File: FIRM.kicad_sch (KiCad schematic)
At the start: 93 parts, among them J1 DM3CS-SF, J2 Conn_01x02_Pin, Q1 IRLML6402, U1 W25Q128JVP, U2 STM32F405RGTx, U3 ADXL371, U5 INA219AxDCN, U6 MIC5219-3.3YM5, U9 A-USBC-20F0-EA-GSR05, X1 32.768khz, Y1 12 MHz

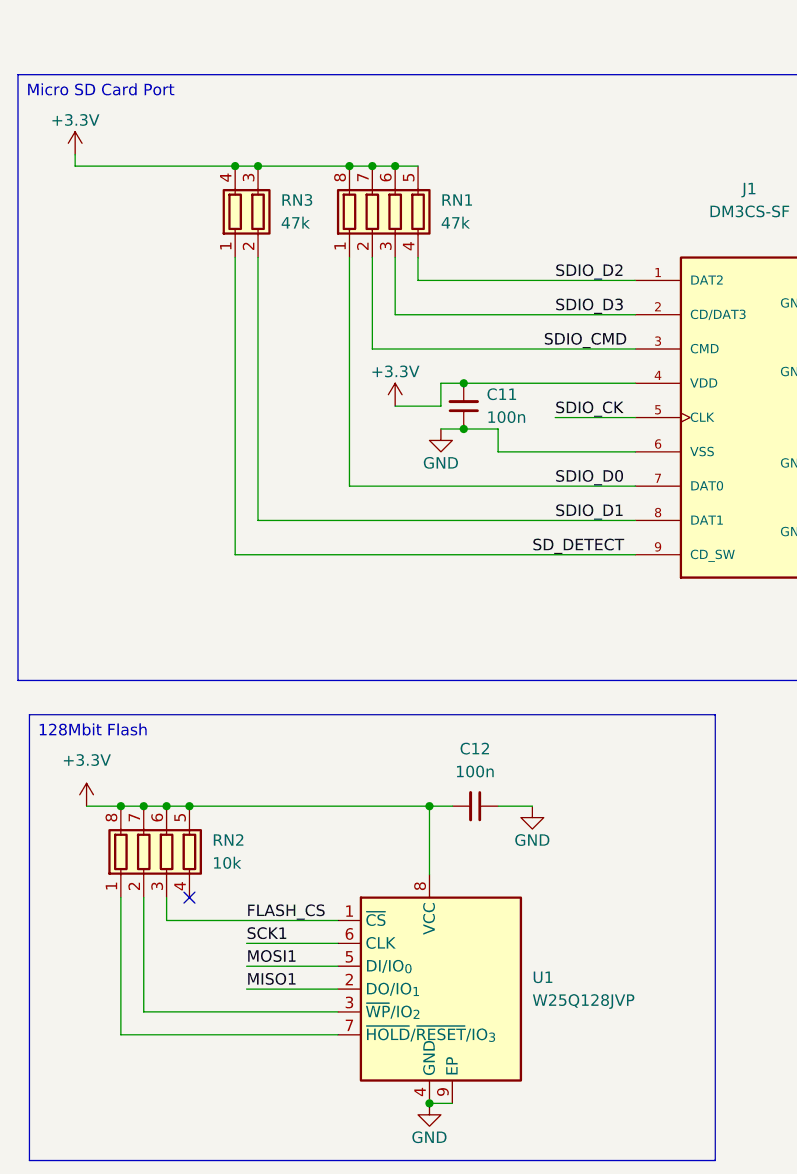
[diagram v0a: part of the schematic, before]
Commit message: cleanup and improved decoupling capacitor locations
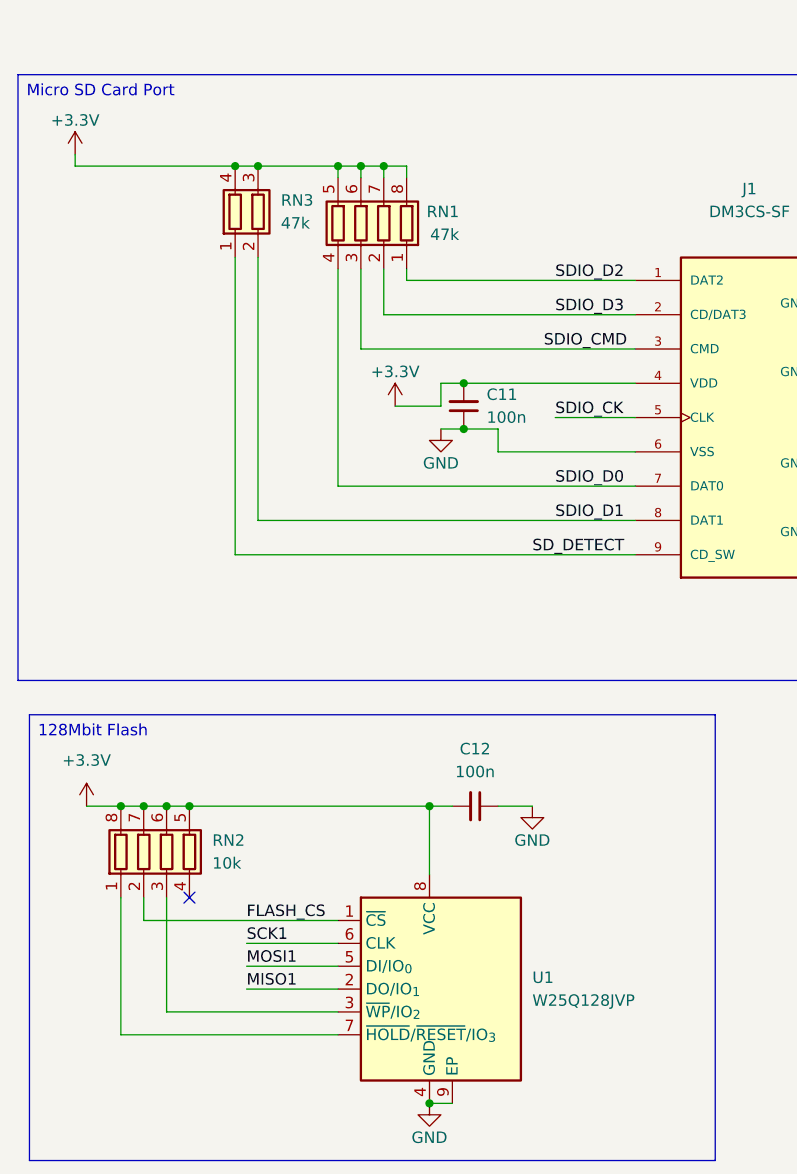
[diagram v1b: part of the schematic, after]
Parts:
- U1: footprint Package_SON:WSON-8-1EP_6x5mm_P1.27mm_EP3.4x4.3mm -> Package_SO:SOIC-8_5.3x5.3mm_P1.27mm
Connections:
- net FLASH_CS: now also RN2.2 (R2.1); no longer RN2.3 (R3.1)
- net SDIO_CMD: now also RN1.3 (R3.1); no longer RN1.2 (R2.1)
- net SDIO_D0: now also RN1.4 (R4.1); no longer RN1.1 (R1.1)
- net SDIO_D2: now also RN1.1 (R1.1); no longer RN1.4 (R4.1)
- net SDIO_D3: now also RN1.2 (R2.1); no longer RN1.3 (R3.1)
- net at U1.3 (~{WP}/IO_{2}): now also RN2.3 (R3.1); no longer RN2.2 (R2.1)
- new net: U3.10 (RES), U3.13 (GND), U3.16 (GND)
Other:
- moved on the sheet: RN1

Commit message: added back resistors
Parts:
- removed RN1: 47k, connectors:R_Array_YC104, symbol Device:R_Pack04
- removed RN3: 47k, connectors:R_Array_EXB-24V, symbol Device:R_Pack02
- removed U1: W25Q128JVP, Package_SO:SOIC-8_5.3x5.3mm_P1.27mm, symbol Memory_Flash:W25Q128JVP
- added R1, R2, R4, R5, R6, R7: 47k, Resistor_SMD:R_0402_1005Metric, symbol Device:R_Small
- added U1: W25Q128JVS, Package_SO:SOIC-8_5.3x5.3mm_P1.27mm, symbol Memory_Flash:W25Q128JVS
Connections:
- net +3.3V: now also R1.2, R2.2, R4.2, R5.2, R6.2, R7.2, U1.8 (VCC)
- net FLASH_CS: now also U1.1 (~{CS})
- net GND: now also U1.4 (GND)
- net MISO1: now also U1.2 (DO/IO_{1})
- net MOSI1: now also U1.5 (DI/IO_{0})
- net SCK1: now also U1.6 (CLK)
- net SDIO_CMD: now also R4.1
- net SDIO_D0: now also R5.1
- net SDIO_D1: now also R6.1
- net SDIO_D2: now also R1.1
- net SDIO_D3: now also R2.1
- net SD_DETECT: now also R7.1
- net at RN2.1 (R1.1): now also U1.7 (~{HOLD}/~{RESET}/IO_{3})
- net at RN2.3 (R3.1): now also U1.3 (~{WP}/IO_{2})
- new net: U3.10 (RES), U3.13 (GND), U3.16 (GND)

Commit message: part numbers
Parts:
- C1, C17: value 0.1u -> 100n; Digikey PN 399-C0603C104K5RACTUCT-ND -> 1276-1043-1-ND
- C10, C5: Digikey PN 311-1767-1-ND -> 490-GJM1555C1H140FB01DCT-ND
- C11, C12, C13, C15, C19, C20, C21, C22, C23, C25, C27, C3, C6, C8: Digikey PN 399-C0603C104K5RACTUCT-ND -> 1276-1043-1-ND
- C14, C9: Digikey PN 490-4520-1-ND -> 490-10012-1-ND
- C16: Digikey PN 399-C0603C103K5RACTUCT-ND -> 490-1313-1-ND
- C18, C29: Digikey PN 587-1241-1-ND -> 1276-1067-1-ND
- C2: Digikey PN 1276-1044-1-ND -> 1276-1482-1-ND
- C24, C28, C30: Digikey PN 490-18214-1-ND -> 1276-1451-1-ND
- C26: Digikey PN 1276-1168-1-ND -> 490-1300-1-ND
- C4, C7: Digikey PN 1276-2134-1-ND -> 311-3714-1-ND
- D1: Digikey PN 160-1645-1-ND -> 160-LTST-C281TBKTCT-ND
- D2: Digikey PN 160-1428-1-ND -> 160-LTST-C281KSKTCT-ND
- D3: Digikey PN 160-1422-1-ND -> 160-LTST-C281KRKTCT-ND
- D5: Digikey PN 160-1423-1-ND -> 160-LTST-C281KGKTCT-ND
- R1, R2, R4, R5, R6, R7: Digikey PN 311-2.20KHRCT-ND -> 311-47.0KLRCT-ND
- R11, R12: Digikey PN 311-2.20KHRCT-ND -> P3.3KDCCT-ND
- R13: Digikey PN 311-330HRCT-ND -> 311-330LRCT-ND
- R14, R18: Digikey PN P1.2KDBCT-ND -> 311-1.2KJRCT-ND
- R15: Digikey PN 311-1.50KHRCT-ND -> 311-1.50KLRCT-ND
- R16, R3: Digikey PN 311-100KHRCT-ND -> P100KLCT-ND
- R17: value 0.01R -> 10m; Digikey PN (none) -> P19181CT-ND
- R19: Digikey PN 541-100HCT-ND -> P100LCT-ND
- R20, R21: Digikey PN 311-5.10KHRCT-ND -> P5.1KDCCT-ND
- RN2: Digikey PN (none) -> 13-YC104-FR-0710KLCT-ND
- U1: Digikey PN (none) -> 256-W25Q128JVSIQTRCT-ND
- U3: Digikey PN (none) -> 505-ADXL371BCCZ-RL7CT-ND
- U5: Digikey PN (none) -> 296-23770-1-ND
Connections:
- new net: U3.10 (RES), U3.13 (GND), U3.16 (GND)
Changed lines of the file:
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@@
 			)
 		)
+		(property "Digikey PN" "256-W25Q128JVSIQTRCT-ND"
+			(at 60.96 260.35 0)
+			(effects
+				(font
+					(size 1.27 1.27)
+				)
+				(hide yes)
+			)
+		)
 		(pin "1"
 		)
@@
 			)
 		)
-		(property "Digikey PN" "399-C0603C104K5RACTUCT-ND"
+		(property "Digikey PN" "1276-1043-1-ND"
 			(at 87.63 41.91 0)
 			(effects
@@
 			)
 		)
-		(property "Digikey PN" "399-C0603C104K5RACTUCT-ND"
+		(property "Digikey PN" "1276-1043-1-ND"
 			(at 36.83 41.91 0)
 			(effects
@@
 			)
 		)
-		(property "Digikey PN" "311-100KHRCT-ND"
+		(property "Digikey PN" "P100KLCT-ND"
 			(at 30.48 66.04 0)
 			(effects
@@
 			)
 		)
-		(property "Digikey PN" "490-18214-1-ND"
+		(property "Digikey PN" "1276-1451-1-ND"
 			(at 340.36 224.79 0)
 			(effects
@@
 			)
 		)
-		(property "Value" "0.1u"
+		(property "Value" "100n"
 			(at 22.098 62.23 0)
 			(effects
@@
 			)
 		)
-		(property "Digikey PN" "399-C0603C104K5RACTUCT-ND"
+		(property "Digikey PN" "1276-1043-1-ND"
 			(at 19.05 60.96 0)
 			(effects
@@
 			)
 		)
-		(property "Digikey PN" "399-C0603C104K5RACTUCT-ND"
+		(property "Digikey PN" "1276-1043-1-ND"
 			(at 285.75 105.41 0)
 			(effects
@@
 			)
 		)
-		(property "Digikey PN" "160-1428-1-ND"
+		(property "Digikey PN" "160-LTST-C281KSKTCT-ND"
 			(at 191.77 116.84 0)
 			(effects
@@
 			)
 		)
-		(property "Digikey PN" "399-C0603C104K5RACTUCT-ND"
+		(property "Digikey PN" "1276-1043-1-ND"
 			(at 64.77 195.58 0)
 			(effects
@@
 			)
 		)
-		(property "Digikey PN" "311-2.20KHRCT-ND"
+		(property "Digikey PN" "P3.3KDCCT-ND"
 			(at 153.67 111.76 0)
 			(effects
@@
 			)
 		)
-		(property "Digikey PN" "399-C0603C104K5RACTUCT-ND"
+		(property "Digikey PN" "1276-1043-1-ND"
 			(at 66.04 240.03 90)
 			(effects
@@
 			)
 		)
-		(property "Digikey PN" "399-C0603C104K5RACTUCT-ND"
+		(property "Digikey PN" "1276-1043-1-ND"
 			(at 228.6 102.87 0)
 			(effects
@@
 			)
 		)
-		(property "Digikey PN" "311-1767-1-ND"
+		(property "Digikey PN" "490-GJM1555C1H140FB01DCT-ND"
 			(at 41.91 88.9 0)
 			(effects
@@
 			)
 		)
-		(property "Value" "0.1u"
+		(property "Value" "100n"
 			(at 146.05 43.1799 0)
 			(effects
@@
 			)
 		)
-		(property "Digikey PN" "399-C0603C104K5RACTUCT-ND"
+		(property "Digikey PN" "1276-1043-1-ND"
 			(at 142.24 41.91 0)
 			(effects
@@
 			)
 		)
-		(property "Digikey PN" "311-2.20KHRCT-ND"
+		(property "Digikey PN" "311-47.0KLRCT-ND"
 			(at 54.61 175.26 0)
 			(effects
@@
 			)
 		)
-		(property "Digikey PN" "160-1422-1-ND"
+		(property "Digikey PN" "160-LTST-C281KRKTCT-ND"
 			(at 191.77 128.27 0)
 			(effects
@@
 			)
 		)
-		(property "Digikey PN" "311-330HRCT-ND"
+		(property "Digikey PN" "311-330LRCT-ND"
 			(at 177.8 105.41 90)
 			(effects
@@
 			)
 		)
-		(property "Digikey PN" "311-2.20KHRCT-ND"
+		(property "Digikey PN" "P3.3KDCCT-ND"
 			(at 144.78 111.76 0)
 			(effects
@@
 			)
 		)
-		(property "Digikey PN" "311-1767-1-ND"
+		(property "Digikey PN" "490-GJM1555C1H140FB01DCT-ND"
 			(at 63.5 90.17 0)
 			(effects
@@
 			)
 		)
+		(property "Digikey PN" "13-YC104-FR-0710KLCT-ND"
+			(at 31.75 245.11 0)
+			(effects
+				(font
+					(size 1.27 1.27)
+				)
+				(hide yes)
+			)
+		)
 		(pin "7"
 		)
@@
 			)
 		)
-		(property "Digikey PN" "P1.2KDBCT-ND"
+		(property "Digikey PN" "311-1.2KJRCT-ND"
 			(at 322.58 208.28 0)
 			(effects
@@
 			)
 		)
-		(property "Digikey PN" "311-1.50KHRCT-ND"
+		(property "Digikey PN" "311-1.50KLRCT-ND"
 			(at 177.8 128.27 90)
 			(effects
@@
 			)
 		)
-		(property "Digikey PN" "1276-2134-1-ND"
+		(property "Digikey PN" "311-3714-1-ND"
 			(at 39.37 130.81 0)
 			(effects
@@
 			)
 		)
-		(property "Digikey PN" "311-2.20KHRCT-ND"
+		(property "Digikey PN" "311-47.0KLRCT-ND"
 			(at 24.13 175.26 0)
 			(effects
@@
 			)
 		)
-		(property "Digikey PN" "490-18214-1-ND"
+		(property "Digikey PN" "1276-1451-1-ND"
 			(at 353.06 138.43 90)
 			(effects
@@
 			)
 		)
-		(property "Digikey PN" "541-100HCT-ND"
+		(property "Digikey PN" "P100LCT-ND"
 			(at 379.73 40.64 90)
 			(effects
@@
 			)
 		)
-		(property "Digikey PN" "490-4520-1-ND"
+		(property "Digikey PN" "490-10012-1-ND"
 			(at 73.66 130.81 0)
 			(effects
@@
 			)
 		)
-		(property "Digikey PN" "587-1241-1-ND"
+		(property "Digikey PN" "1276-1067-1-ND"
 			(at 172.72 41.91 0)
 			(effects
@@
 			)
 		)
-		(property "Digikey PN" "399-C0603C104K5RACTUCT-ND"
+		(property "Digikey PN" "1276-1043-1-ND"
 			(at 327.66 27.94 90)
 			(effects
@@
 			)
 		)
-		(property "Digikey PN" "399-C0603C103K5RACTUCT-ND"
+		(property "Digikey PN" "490-1313-1-ND"
 			(at 130.81 41.91 0)
 			(effects
@@
 			)
 		)
-		(property "Digikey PN" "1276-2134-1-ND"
+		(property "Digikey PN" "311-3714-1-ND"
 			(at 50.8 130.81 0)
 			(effects
@@
 			)
 		)
-		(property "Digikey PN" "311-100KHRCT-ND"
+		(property "Digikey PN" "P100KLCT-ND"
 			(at 243.84 222.25 0)
 			(effects
@@
 			)
 		)
-		(property "Digikey PN" "311-2.20KHRCT-ND"
+		(property "Digikey PN" "311-47.0KLRCT-ND"
 			(at 46.99 175.26 0)
 			(effects
@@
 			)
 		)
-		(property "Digikey PN" "311-2.20KHRCT-ND"
+		(property "Digikey PN" "311-47.0KLRCT-ND"
 			(at 39.37 175.26 0)
 			(effects
@@
 			)
 		)
-		(property "Digikey PN" "160-1423-1-ND"
+		(property "Digikey PN" "160-LTST-C281KGKTCT-ND"
 			(at 326.39 201.93 0)
 			(effects
@@
 			)
 		)
-		(property "Digikey PN" "311-2.20KHRCT-ND"
+		(property "Digikey PN" "311-47.0KLRCT-ND"
 			(at 62.23 175.26 0)
 			(effects
@@
 			)
 		)
-		(property "Digikey PN" "399-C0603C104K5RACTUCT-ND"
+		(property "Digikey PN" "1276-1043-1-ND"
 			(at 48.26 41.91 0)
 			(effects
@@
 			)
 		)
-		(property "Digikey PN" "490-18214-1-ND"
+		(property "Digikey PN" "1276-1451-1-ND"
 			(at 299.72 218.44 0)
 			(effects
@@
 			)
 		)
-		(property "Digikey PN" "311-2.20KHRCT-ND"
+		(property "Digikey PN" "311-47.0KLRCT-ND"
 			(at 31.75 175.26 0)
 			(effects
@@
 			)
 		)
-		(property "Digikey PN" "160-1645-1-ND"
+		(property "Digikey PN" "160-LTST-C281TBKTCT-ND"
 			(at 191.77 105.41 0)
 			(effects
@@
 			)
 		)
-		(property "Digikey PN" "399-C0603C104K5RACTUCT-ND"
+		(property "Digikey PN" "1276-1043-1-ND"
 			(at 320.04 27.94 90)
 			(effects
@@
 			)
 		)
-		(property "Digikey PN" "399-C0603C104K5RACTUCT-ND"
+		(property "Digikey PN" "1276-1043-1-ND"
 			(at 241.3 102.87 0)
 			(effects
@@
 			)
 		)
-		(property "Digikey PN" "311-5.10KHRCT-ND"
+		(property "Digikey PN" "P5.1KDCCT-ND"
 			(at 394.97 193.04 90)
 			(effects
@@
 			)
 		)
-		(property "Digikey PN" "311-5.10KHRCT-ND"
+		(property "Digikey PN" "P5.1KDCCT-ND"
 			(at 388.62 190.5 90)
 			(effects
@@
 			)
 		)
-		(property "Digikey PN" "587-1241-1-ND"
+		(property "Digikey PN" "1276-1067-1-ND"
 			(at 350.52 148.59 0)
 			(effects
@@
 			)
 		)
-		(property "Value" "0.01R"
+		(property "Value" "10m"
 			(at 270.002 120.65 0)
 			(effects
@@
 			)
 		)
+		(property "Digikey PN" "P19181CT-ND"
+			(at 267.97 119.38 0)
+			(effects
+				(font
+					(size 1.27 1.27)
+				)
+				(hide yes)
+			)
+		)
 		(pin "2"
 		)
@@
 			)
 		)
-		(property "Digikey PN" "399-C0603C104K5RACTUCT-ND"
+		(property "Digikey PN" "1276-1043-1-ND"
 			(at 73.66 41.91 0)
 			(effects
@@
 			)
 		)
-		(property "Digikey PN" "1276-1044-1-ND"
+		(property "Digikey PN" "1276-1482-1-ND"
 			(at 22.86 41.91 0)
 			(effects
@@
 			)
 		)
-		(property "Digikey PN" "P1.2KDBCT-ND"
+		(property "Digikey PN" "311-1.2KJRCT-ND"
 			(at 177.8 116.84 90)
 			(effects
@@
 			)
 		)
+		(property "Digikey PN" "296-23770-1-ND"
+			(at 297.18 119.38 0)
+			(effects
+				(font
+					(size 1.27 1.27)
+				)
+				(hide yes)
+			)
+		)
 		(pin "8"
 		)
@@
 			)
 		)
-		(property "Digikey PN" "399-C0603C104K5RACTUCT-ND"
+		(property "Digikey PN" "1276-1043-1-ND"
 			(at 254 76.2 0)
 			(effects
@@
 			)
 		)
-		(property "Digikey PN" "490-4520-1-ND"
+		(property "Digikey PN" "490-10012-1-ND"
 			(at 62.23 130.81 0)
 			(effects
@@
 			)
 		)
-		(property "Digikey PN" "399-C0603C104K5RACTUCT-ND"
+		(property "Digikey PN" "1276-1043-1-ND"
 			(at 60.96 41.91 0)
 			(effects
@@
 			)
 		)
+		(property "Digikey PN" "505-ADXL371BCCZ-RL7CT-ND"
+			(at 234.95 120.65 0)
+			(effects
+				(font
+					(size 1.27 1.27)
+				)
+				(hide yes)
+			)
+		)
 		(pin "8"
 		)
@@
 			)
 		)
-		(property "Digikey PN" "1276-1168-1-ND"
+		(property "Digikey PN" "490-1300-1-ND"
 			(at 322.58 222.25 0)
 			(effects
@@
 			)
 		)
-		(property "Digikey PN" "399-C0603C104K5RACTUCT-ND"
+		(property "Digikey PN" "1276-1043-1-ND"
 			(at 264.16 76.2 0)
 			(effects

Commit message: get stuff ready
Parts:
- removed TP10: I2C1_SCL Test Point, connectors:smd_test_pads_1mm, symbol Connector:TestPoint
- removed TP11: I2C1_SDA Test Point, connectors:smd_test_pads_1mm, symbol Connector:TestPoint
- removed TP15: GND Test Point, connectors:Testpoint_1.5x1.5mm_1.0mm, symbol Connector:TestPoint
- removed TP16: IMU_CS Test Point, connectors:smd_test_pads_1mm, symbol Connector:TestPoint
- removed TP17: BMP_CS Test Point, connectors:smd_test_pads_1mm, symbol Connector:TestPoint
- removed TP18: MAG_CS Test Point, connectors:smd_test_pads_1mm, symbol Connector:TestPoint
- removed TP19: HIG_CS Test Point, connectors:smd_test_pads_1mm, symbol Connector:TestPoint
- removed TP20: IMU_INT Test Point, connectors:smd_test_pads_1mm, symbol Connector:TestPoint
- removed TP21: BMP_INT Test Point, connectors:smd_test_pads_1mm, symbol Connector:TestPoint
- removed TP22: MAG_INT Test Point, connectors:smd_test_pads_1mm, symbol Connector:TestPoint
- removed TP23: HIG_INT Test Point, connectors:smd_test_pads_1mm, symbol Connector:TestPoint
- removed TP6: PA4 Test Point, connectors:smd_test_pads_1mm, symbol Connector:TestPoint
- removed TP7: MOSI2 Test Point, connectors:smd_test_pads_1mm, symbol Connector:TestPoint
- removed TP8: MISO2 Test Point, connectors:smd_test_pads_1mm, symbol Connector:TestPoint
- removed TP9: SCK2 Test Point, connectors:smd_test_pads_1mm, symbol Connector:TestPoint
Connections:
- new net: U3.10 (RES), U3.13 (GND), U3.16 (GND)

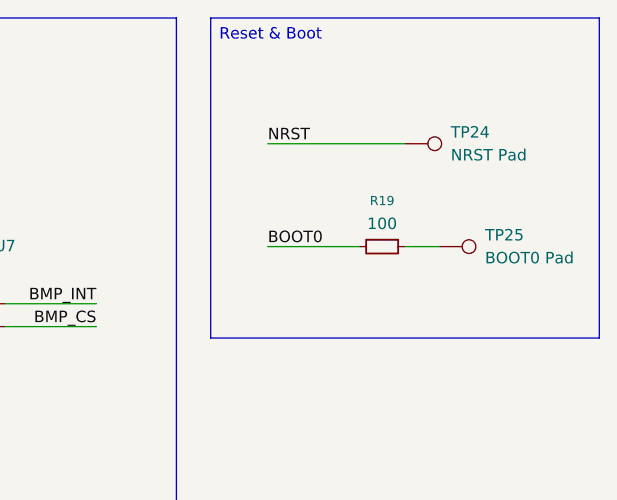
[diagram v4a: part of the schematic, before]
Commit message: Initial Six Layer
Stackup is right board recommended in this video: https://youtu.be/ySuUZEjARPY?t=6617
.
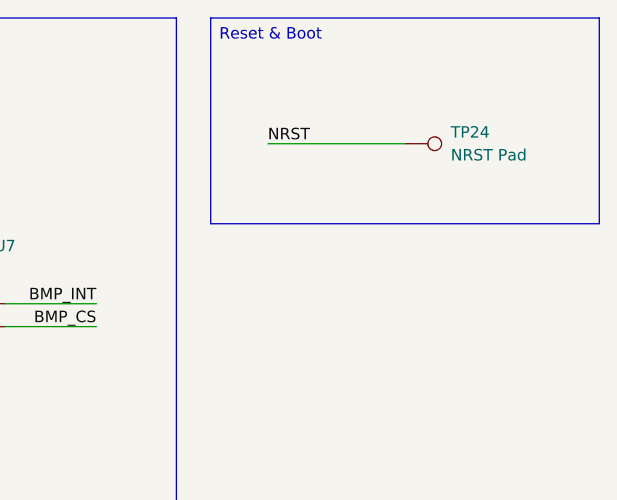
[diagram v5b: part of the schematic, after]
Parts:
- removed R19: 100, Resistor_SMD:R_0402_1005Metric, symbol Device:R_Small
- removed TP25: BOOT0 Pad, connectors:smd_test_pads_1mm, symbol Connector:TestPoint
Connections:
- new net: U3.10 (RES), U3.13 (GND), U3.16 (GND)
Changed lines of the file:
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@@
 		(exclude_from_sim no)
 		(at 360.68 15.24 0)
-		(size 43.18 35.56)
+		(size 43.18 22.86)
 		(margins 0.9525 0.9525 0.9525 0.9525)
 		(stroke
@@
 	(wire
 		(pts
-			(xy 382.27 40.64) (xy 386.08 40.64)
-		)
-		(stroke
-			(width 0)
-			(type default)
-		)
-	)
-	(wire
-		(pts
 			(xy 127 88.9) (xy 166.37 88.9)
 		)
@@
 	(wire
 		(pts
-			(xy 367.03 40.64) (xy 377.19 40.64)
-		)
-		(stroke
-			(width 0)
-			(type default)
-		)
-	)
-	(wire
-		(pts
 			(xy 127 132.08) (xy 138.43 132.08)
 		)
@@
 		)
 	)
-	(label "BOOT0"
-		(at 367.03 40.64 0)
-		(effects
-			(font
-				(size 1.27 1.27)
-			)
-			(justify left bottom)
-		)
-	)
 	(label "SDIO_CMD"
 		(at 73.66 189.23 0)
@@
 	)
 	(symbol
-		(lib_id "Connector:TestPoint")
-		(at 386.08 40.64 270)
-		(unit 1)
-		(exclude_from_sim no)
-		(in_bom no)
-		(on_board yes)
-		(dnp no)
-		(property "Reference" "TP25"
-			(at 391.16 39.3699 90)
-			(effects
-				(font
-					(size 1.27 1.27)
-				)
-				(justify left)
-			)
-		)
-		(property "Value" "BOOT0 Pad"
-			(at 391.16 41.9099 90)
-			(effects
-				(font
-					(size 1.27 1.27)
-				)
-				(justify left)
-			)
-		)
-		(property "Footprint" "connectors:smd_test_pads_1mm"
-			(at 386.08 45.72 0)
-			(effects
-				(font
-					(size 1.27 1.27)
-				)
-				(hide yes)
-			)
-		)
-		(property "Datasheet" "~"
-			(at 386.08 45.72 0)
-			(effects
-				(font
-					(size 1.27 1.27)
-				)
-				(hide yes)
-			)
-		)
-		(property "Description" "test point"
-			(at 386.08 40.64 0)
-			(effects
-				(font
-					(size 1.27 1.27)
-				)
-				(hide yes)
-			)
-		)
-		(property "Digikey PN" ""
-			(at 386.08 40.64 90)
-			(effects
-				(font
-					(size 1.27 1.27)
-				)
-				(hide yes)
-			)
-		)
-		(pin "1"
-		)
-		(instances
-			(project ""
-				(path "/d3f8a00a-ef65-439d-87f3-373a106a7ddb"
-					(reference "TP25")
-					(unit 1)
-				)
-			)
-		)
-	)
-	(symbol
 		(lib_id "Device:R_Small")
 		(at 177.8 105.41 270)
@@
 					(unit 1)
 				)
-			)
-		)
-	)
-	(symbol
-		(lib_id "Device:R_Small")
-		(at 379.73 40.64 270)
-		(unit 1)
-		(exclude_from_sim no)
-		(in_bom yes)
-		(on_board yes)
-		(dnp no)
-		(fields_autoplaced yes)
-		(property "Reference" "R19"
-			(at 379.73 35.56 90)
-			(effects
-				(font
-					(size 1.016 1.016)
-				)
-			)
-		)
-		(property "Value" "100"
-			(at 379.73 38.1 90)
-			(effects
-				(font
-					(size 1.27 1.27)
-				)
-			)
-		)
-		(property "Footprint" "Resistor_SMD:R_0402_1005Metric"
-			(at 379.73 40.64 0)
-			(effects
-				(font
-					(size 1.27 1.27)
-				)
-				(hide yes)
-			)
-		)
-		(property "Datasheet" "~"
-			(at 379.73 40.64 0)
-			(effects
-				(font
-					(size 1.27 1.27)
-				)
-				(hide yes)
-			)
-		)
-		(property "Description" "Resistor, small symbol"
-			(at 379.73 40.64 0)
-			(effects
-				(font
-					(size 1.27 1.27)
-				)
-				(hide yes)
-			)
-		)
-		(property "MPN" "C177347"
-			(at 379.73 40.64 90)
-			(effects
-				(font
-					(size 1.27 1.27)
-				)
-				(hide yes)
-			)
-		)
-		(property "Digikey PN" "P100LCT-ND"
-			(at 379.73 40.64 90)
-			(effects
-				(font
-					(size 1.27 1.27)
-				)
-				(hide yes)
-			)
-		)
-		(pin "2"
-		)
-		(pin "1"
-		)
-		(instances
-			(project "FIRM"
-				(path "/d3f8a00a-ef65-439d-87f3-373a106a7ddb"
-					(reference "R19")
-					(unit 1)
-				)
